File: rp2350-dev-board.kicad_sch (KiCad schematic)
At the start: 49 parts, among them J1 USB4105-GF-A, J2 Conn_02x20_Odd_Even, J3 Conn_02x20_Odd_Even, SW1 RST, SW2 BOOTSEL, U1 W25Q128JVS, U2 RP2350B, U3 TPS6285021HQDRLRQ1, U4 LM66100DCK, Y1 ABM8-272-T3 12MHz/10pF

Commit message: initial layout
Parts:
- J2: value Conn_02x20_Odd_Even -> EXT1
- J3: value Conn_02x20_Odd_Even -> EXT2
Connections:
- net +3.3V: no longer J3.26 (Pin_26), J3.28 (Pin_28), J3.30 (Pin_30), J3.32 (Pin_32)
- net +5V: now also U4.3 (~{CE}); no longer J3.2 (Pin_2), J3.4 (Pin_4), J3.6 (Pin_6), J3.8 (Pin_8)
- net BOOTSEL#: no longer J3.23 (Pin_23)
- net GND: no longer J3.34 (Pin_34), J3.36 (Pin_36), J3.38 (Pin_38), J3.40 (Pin_40), U4.3 (~{CE})
- net GPIO0: no longer J2.1 (Pin_1)
- net GPIO1: no longer J2.3 (Pin_3)
- net GPIO10: now also J2.25 (Pin_25); no longer J2.21 (Pin_21)
- net GPIO11: now also J2.28 (Pin_28); no longer J2.23 (Pin_23)
- net GPIO12: now also J2.27 (Pin_27); no longer J2.25 (Pin_25)
- net GPIO13: now also J2.30 (Pin_30); no longer J2.27 (Pin_27)
- net GPIO15: now also J2.32 (Pin_32); no longer J2.31 (Pin_31)
- net GPIO16: now also J2.31 (Pin_31); no longer J2.33 (Pin_33)
- net GPIO17: now also J2.34 (Pin_34); no longer J2.35 (Pin_35)
- net GPIO18: now also J2.33 (Pin_33); no longer J2.37 (Pin_37)
- net GPIO19: now also J2.36 (Pin_36); no longer J2.39 (Pin_39)
- net GPIO2: no longer J2.5 (Pin_5)
- net GPIO20: now also J2.35 (Pin_35); no longer J2.2 (Pin_2)
- net GPIO21: now also J3.36 (Pin_36); no longer J2.4 (Pin_4)
- net GPIO22: now also J3.35 (Pin_35); no longer J2.6 (Pin_6)
- net GPIO23: now also J3.34 (Pin_34); no longer J2.8 (Pin_8)
- net GPIO24: now also J3.33 (Pin_33); no longer J2.10 (Pin_10)
- net GPIO25: now also J3.32 (Pin_32); no longer J2.12 (Pin_12)
- net GPIO26: now also J3.31 (Pin_31); no longer J2.14 (Pin_14)
- net GPIO27: now also J3.30 (Pin_30); no longer J2.16 (Pin_16)
- net GPIO28: now also J3.25 (Pin_25); no longer J2.18 (Pin_18)
- net GPIO29: now also J3.24 (Pin_24); no longer J2.20 (Pin_20)
- net GPIO3: no longer J2.7 (Pin_7)
- net GPIO30: now also J3.23 (Pin_23); no longer J2.22 (Pin_22)
- net GPIO31: now also J3.22 (Pin_22); no longer J2.24 (Pin_24)
- net GPIO32: now also J3.21 (Pin_21); no longer J2.26 (Pin_26)
- net GPIO33: now also J3.20 (Pin_20); no longer J2.28 (Pin_28)
- net GPIO34: now also J3.19 (Pin_19); no longer J2.30 (Pin_30)
- net GPIO35: now also J3.18 (Pin_18); no longer J2.32 (Pin_32)
- net GPIO36: now also J3.17 (Pin_17); no longer J2.34 (Pin_34)
- net GPIO37: now also J3.16 (Pin_16); no longer J2.36 (Pin_36)
- net GPIO38: now also J3.15 (Pin_15); no longer J2.38 (Pin_38)
- net GPIO39: now also J3.14 (Pin_14); no longer J2.40 (Pin_40)
- net GPIO4: now also J2.15 (Pin_15); no longer J2.9 (Pin_9)
- net GPIO40: now also J3.13 (Pin_13); no longer J3.7 (Pin_7)
- net GPIO41: now also J3.12 (Pin_12); no longer J3.9 (Pin_9)
- net GPIO43: now also J3.10 (Pin_10); no longer J3.13 (Pin_13)
- net GPIO44: now also J3.9 (Pin_9); no longer J3.15 (Pin_15)
- net GPIO45: now also J3.8 (Pin_8); no longer J3.17 (Pin_17)
- net GPIO46: now also J3.7 (Pin_7); no longer J3.19 (Pin_19)
- net GPIO47: now also J3.6 (Pin_6); no longer J3.21 (Pin_21)
- net GPIO5: now also J2.18 (Pin_18); no longer J2.11 (Pin_11)
- net GPIO6: now also J2.17 (Pin_17); no longer J2.13 (Pin_13)
- net GPIO7: now also J2.20 (Pin_20); no longer J2.15 (Pin_15)
- net GPIO8: now also J2.19 (Pin_19); no longer J2.17 (Pin_17)
- net GPIO9: now also J2.26 (Pin_26); no longer J2.19 (Pin_19)
- net RUN: now also J3.26 (Pin_26); no longer J3.5 (Pin_5)
- net SWCLK: now also J3.27 (Pin_27); no longer J3.1 (Pin_1)
- net SWDIO: now also J3.29 (Pin_29); no longer J3.3 (Pin_3)
- no-connect marks 19 -> 3

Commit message: wip
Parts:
- added C28: 100nF, Capacitor_SMD:C_0402_1005Metric_Pad0.74x0.62mm_HandSolder, symbol Device:C_Small
- added D2: GREEN 2.1V 20mA, LED_SMD:LED_0805_2012Metric_Pad1.15x1.40mm_HandSolder, symbol Device:LED_Small
- added R10: 1K, Resistor_SMD:R_0805_2012Metric_Pad1.20x1.40mm_HandSolder, symbol Device:R_Small
- added R11: 10K, Resistor_SMD:R_0805_2012Metric_Pad1.20x1.40mm_HandSolder, symbol Device:R_Small
- added U5: APS6404L-3SQRx-SN, Package_SO:SOIC-8_3.9x4.9mm_P1.27mm, symbol Memory_RAM:APS6404L-3SQRx-SN
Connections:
- net +3.3V: now also C28.1, R11.2, U5.8 (VDD)
- net GND: now also C28.2, D2.1 (K), U5.4 (VSS)
- net GPIO28: now also R10.1
- net GPIO47: now also R11.1, U5.1 (~{CE})
- net QSPI_SCLK: now also U5.6 (SCLK)
- net QSPI_SD0: now also U5.5 (SI/SIO0)
- net QSPI_SD1: now also U5.2 (SO/SIO1)
- net QSPI_SD2: now also U5.3 (SIO2)
- net QSPI_SD3: now also U5.7 (SIO3)
- new net: D2.2 (A), R10.2
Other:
- moved on the sheet: C11, C2, C3, C4, C6, C8, C9, D1, J2, J3, L2, R4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

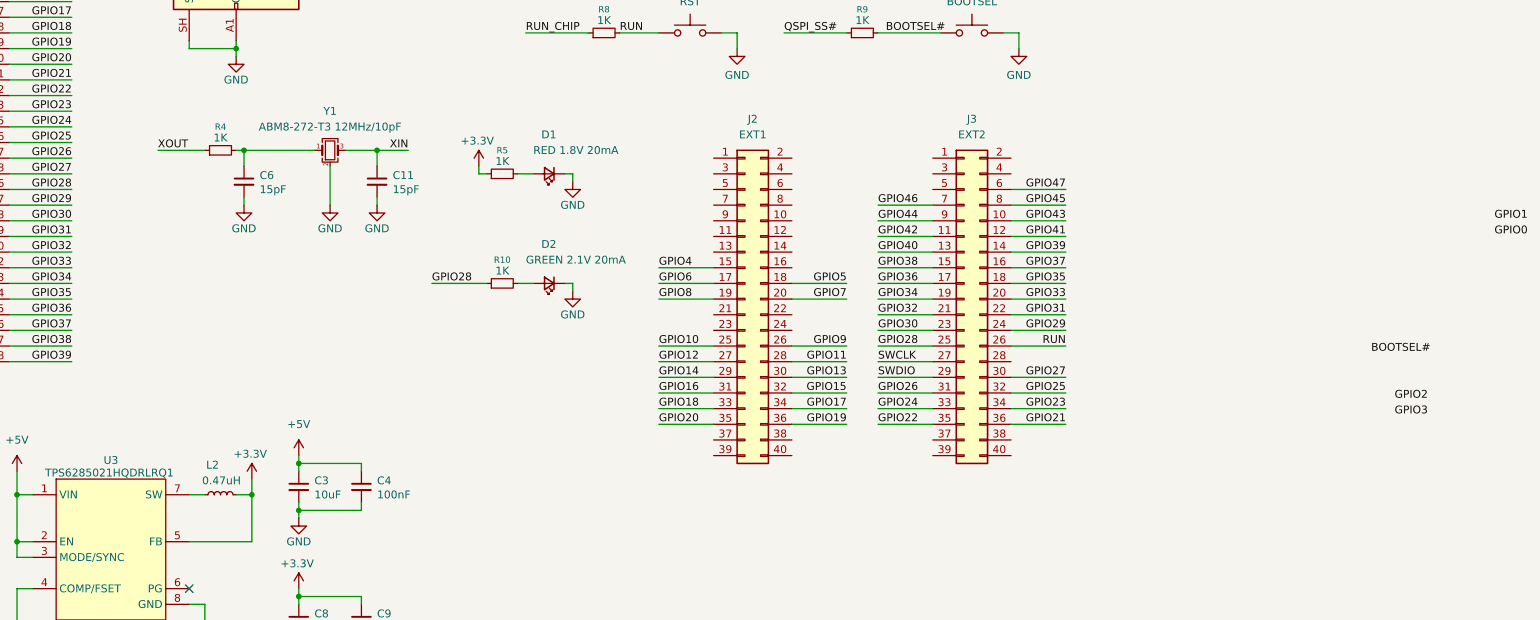
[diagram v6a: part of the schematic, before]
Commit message: add gnd and power to headers
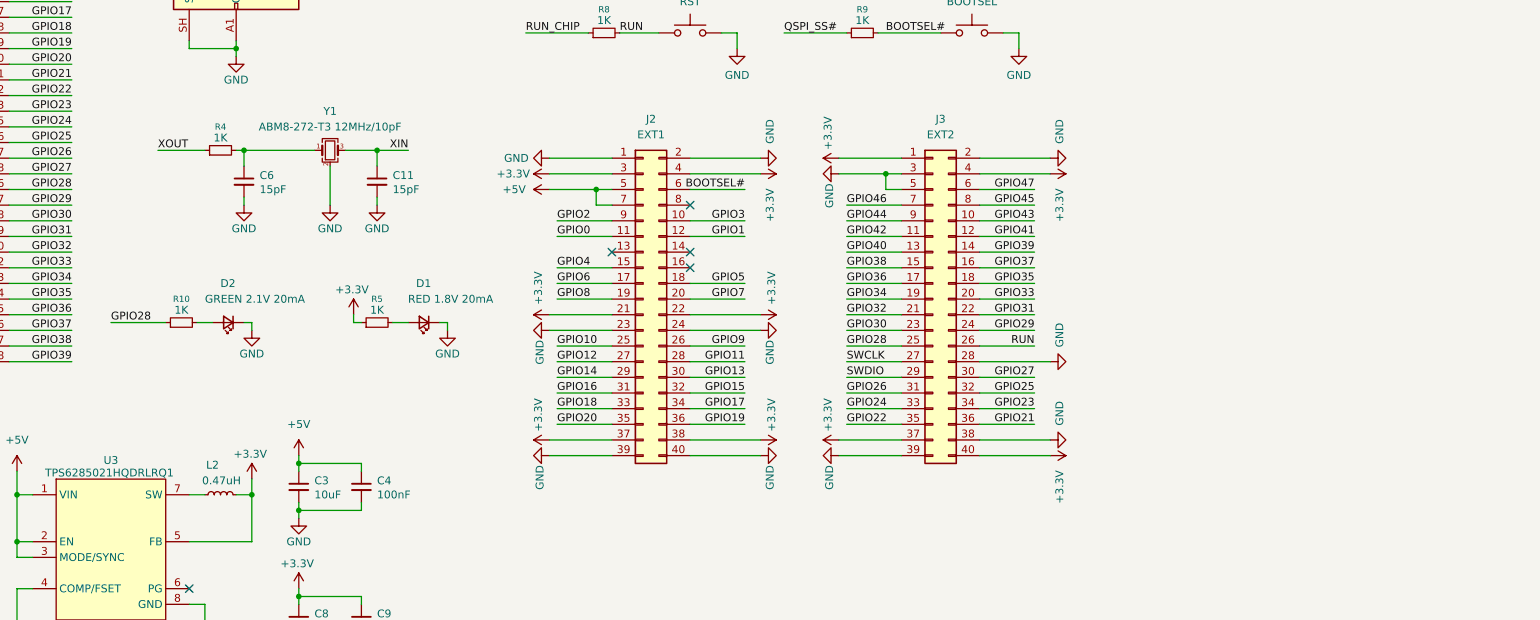
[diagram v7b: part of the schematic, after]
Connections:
- net +3.3V: now also J2.21 (Pin_21), J2.22 (Pin_22), J2.3 (Pin_3), J2.37 (Pin_37), J2.38 (Pin_38), J2.4 (Pin_4), J3.1 (Pin_1), J3.37 (Pin_37), J3.4 (Pin_4), J3.40 (Pin_40)
- net +5V: now also J2.5 (Pin_5), J2.7 (Pin_7)
- net BOOTSEL#: now also J2.6 (Pin_6)
- net GND: now also J2.1 (Pin_1), J2.2 (Pin_2), J2.23 (Pin_23), J2.24 (Pin_24), J2.39 (Pin_39), J2.40 (Pin_40), J3.2 (Pin_2), J3.28 (Pin_28), J3.3 (Pin_3), J3.38 (Pin_38), J3.39 (Pin_39), J3.5 (Pin_5)
- net GPIO0: now also J2.11 (Pin_11)
- net GPIO1: now also J2.12 (Pin_12)
- net GPIO2: now also J2.9 (Pin_9)
- net GPIO3: now also J2.10 (Pin_10)
- no-connect marks 3 -> 7
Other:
- moved on the sheet: D1, D2, J2, J3, R10, R5
